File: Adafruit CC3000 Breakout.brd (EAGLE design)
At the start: 39 x 53 mm, 34 parts, among them IC1 ATmega1284P, U1 CC3000MOD, X1 2500AT44M0400E

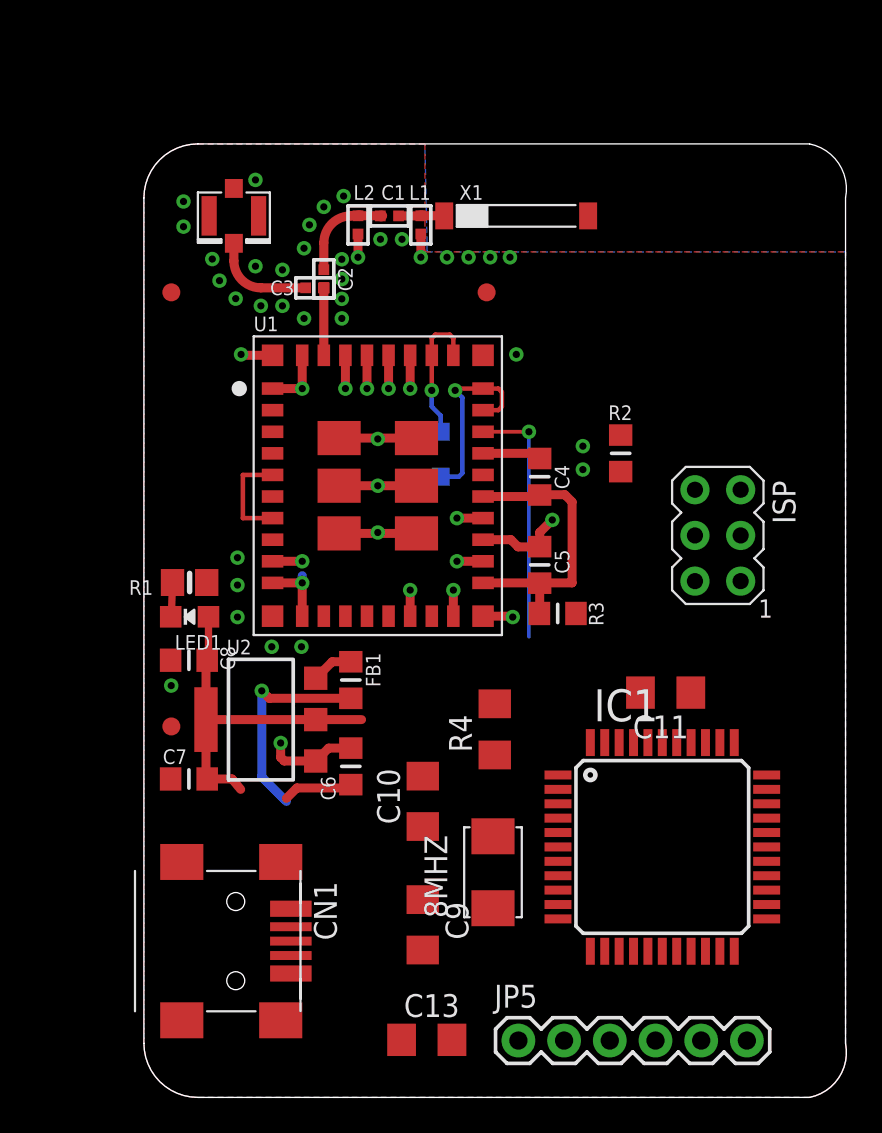
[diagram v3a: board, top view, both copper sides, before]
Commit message: Replace passives (w/ 1206), re-layout components.
Also, change pinouts on the ATmega1284P to match the Wicked Devices
Wildfire prototyping board. Remove rounded corners.
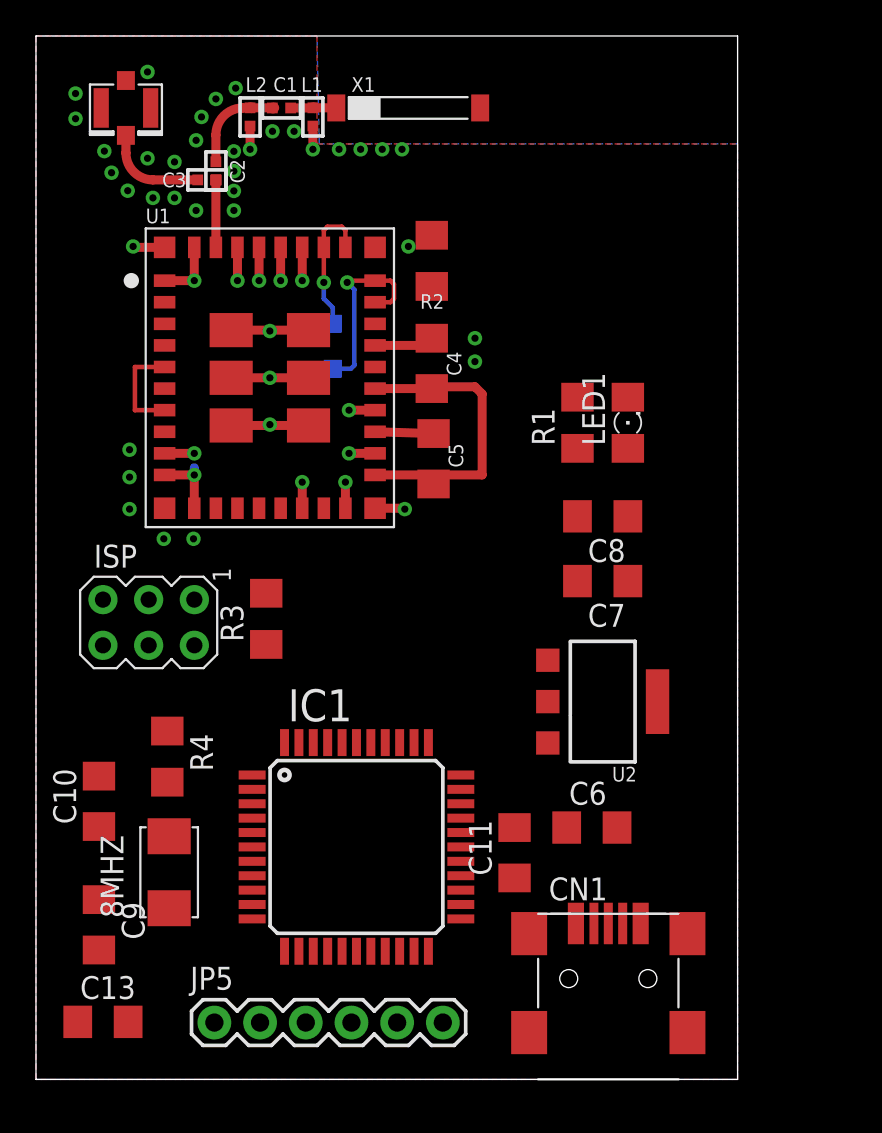
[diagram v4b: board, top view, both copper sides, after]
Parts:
- removed FB1: (no value), microbuilder:_0805MP
- removed FID1, FID2, FID3: FIDUCIAL"", microbuilder:FIDUCIAL_1MM
- C4, C5, C6, C7, C8: device microbuilder:_0805MP -> rcl:C1206
- LED1: device microbuilder:CHIPLED_0805_NOOUTLINE -> led:1206
- R1: device microbuilder:0805-NO -> rcl:R1206
- R2, R3: device microbuilder:_0805MP -> rcl:R1206
- moved ISP 32.0 mm to (6.26, 25.9), turned to 270 degrees
- moved LED1 26.6 mm to (32.9, 37.0)
- moved C7 25.5 mm to (31.5, 28.2)
- moved C8 24.4 mm to (31.5, 31.8)
- moved CN1 23.4 mm to (31.8, 3.83), turned to 0 degrees
- moved R1 23.3 mm to (30.1, 37.0), turned to 90 degrees
- moved U2 19.0 mm to (31.5, 21.5), turned to 270 degrees
- moved R4 18.3 mm to (7.30, 18.4), turned to 270 degrees
- moved C13 18.0 mm to (3.72, 3.70)
- moved 8MHZ 18.0 mm to (7.40, 12.0)
- moved C10 18.0 mm to (3.50, 16.0)
- moved C9 18.0 mm to (3.50, 9.09)
- moved IC1 17.0 mm to (17.8, 13.4)
- moved JP5 16.9 mm to (9.92, 3.66)
- moved R3 16.2 mm to (12.8, 26.1), turned to 90 degrees
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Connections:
- removed net N$9: FB1.2, U2.3
- net SPI_CS_3V: now also IC1.40; no longer IC1.22
- net VBAT_EN_3V: now also IC1.41; no longer IC1.23
- net VIN: now also U2.3; no longer FB1.1
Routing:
- net VBAT: track 36.5 -> 17.2 mm
- net VIN: track 15.7 -> 0.00 mm, vias 1 -> 0
- net VBAT_EN_3V: track 13.9 -> 0.00 mm, vias 1 -> 0
- net GND: track 54.7 -> 47.9 mm, vias 54 -> 51
- net N$9: track 2.33 -> 0.00 mm
- net N$7: track 2.07 -> 0.00 mm
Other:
- board size 39 x 53 mm -> 39 x 58 mm

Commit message: Route board.
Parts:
- moved JP5 2.00 mm to (7.92, 3.66)
- moved C11 0.40 mm to (26.2, 13.1)
- moved R2 0.40 mm to (22.4, 46.0)
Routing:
- net VBAT: track 17.2 -> 106.3 mm, vias 0 -> 2
- net VBAT_EN_3V: track 0.00 -> 44.2 mm, vias 0 -> 2
- net RESET: track 0.00 -> 35.4 mm
- net SPI_CLK_3V: track 0.00 -> 30.1 mm, vias 0 -> 2
- net VIN: track 0.00 -> 30.0 mm
- net SPI_MOSI_3V: track 0.00 -> 21.2 mm, vias 0 -> 2
- net SPI_MISO_3V: track 0.00 -> 20.4 mm, vias 0 -> 2
- net SPI_CS_3V: track 0.00 -> 17.9 mm
- net SPI_IRQ_3V: track 0.00 -> 14.3 mm, vias 0 -> 2
- net N$8: track 0.00 -> 10.6 mm
- net N$10: track 0.00 -> 10.3 mm
- net RX: track 0.00 -> 8.22 mm
- net TX: track 0.00 -> 7.62 mm
- net GND: track 47.9 -> 53.7 mm, vias 51 -> 55
- net DTR: track 0.00 -> 2.86 mm
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
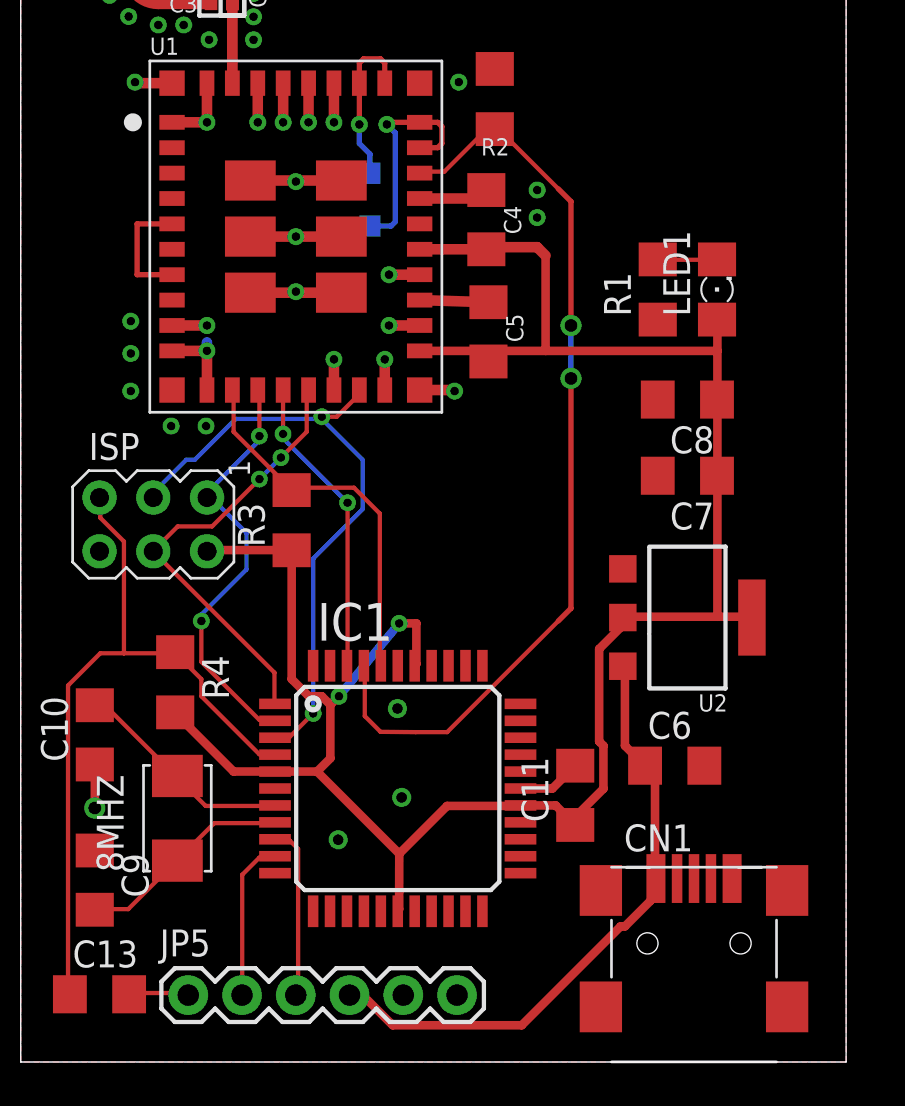
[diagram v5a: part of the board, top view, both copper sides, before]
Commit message: Breakout some microcontroller pins.
Partly un-route the board.
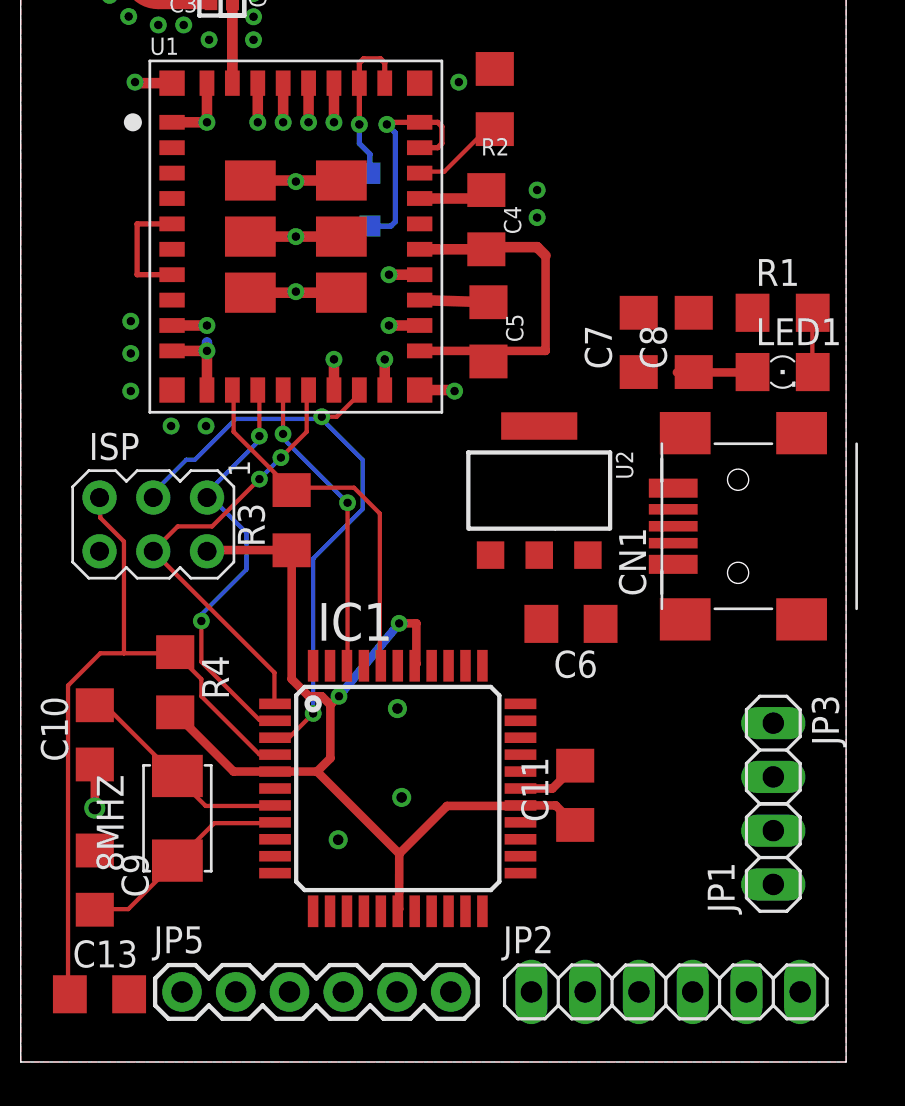
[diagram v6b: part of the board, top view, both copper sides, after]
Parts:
- added JP1, JP3: (no value), pinhead:1X02
- added JP2: (no value), pinhead:1X06
- moved CN1 22.4 mm to (36.2, 25.8), turned to 90 degrees
- moved U2 9.22 mm to (24.5, 27.5), turned to 0 degrees
- moved C6 8.30 mm to (26.0, 21.2), turned to 180 degrees
- moved C7 6.71 mm to (29.2, 34.5), turned to 90 degrees
- moved R1 6.00 mm to (36.0, 35.9), turned to 0 degrees
- moved LED1 4.98 mm to (36.0, 33.1), turned to 0 degrees
- moved C8 2.72 mm to (31.8, 34.5), turned to 90 degrees
- moved JP5 0.33 mm to (7.62, 3.81)
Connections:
- removed net 10: IC1.11
- removed net 11: IC1.12
- removed net 12: IC1.13
- removed net 13: IC1.14
- removed net 16: IC1.19
- removed net 17: IC1.20
- removed net A0: IC1.37
- removed net A1: IC1.36
- new net N$11: IC1.11, JP2.1
- new net N$12: IC1.12, JP2.2
- new net N$13: IC1.13, JP2.3
- new net N$14: IC1.14, JP2.4
- new net N$15: IC1.15, JP2.5
- new net N$16: IC1.16, JP2.6
- new net N$17: IC1.31, JP3.1
- new net N$18: IC1.30, JP3.2
- new net N$5: IC1.19, JP1.1
- new net N$9: IC1.20, JP1.2
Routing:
- net VBAT_EN_3V: track 44.2 -> 4.39 mm, vias 2 -> 0
- net VBAT: track 106.3 -> 70.7 mm
- net VIN: track 30.0 -> 0.00 mm
- net RX: track 8.22 -> 0.00 mm
- net TX: track 7.62 -> 0.00 mm
- net DTR: track 2.86 -> 0.00 mm

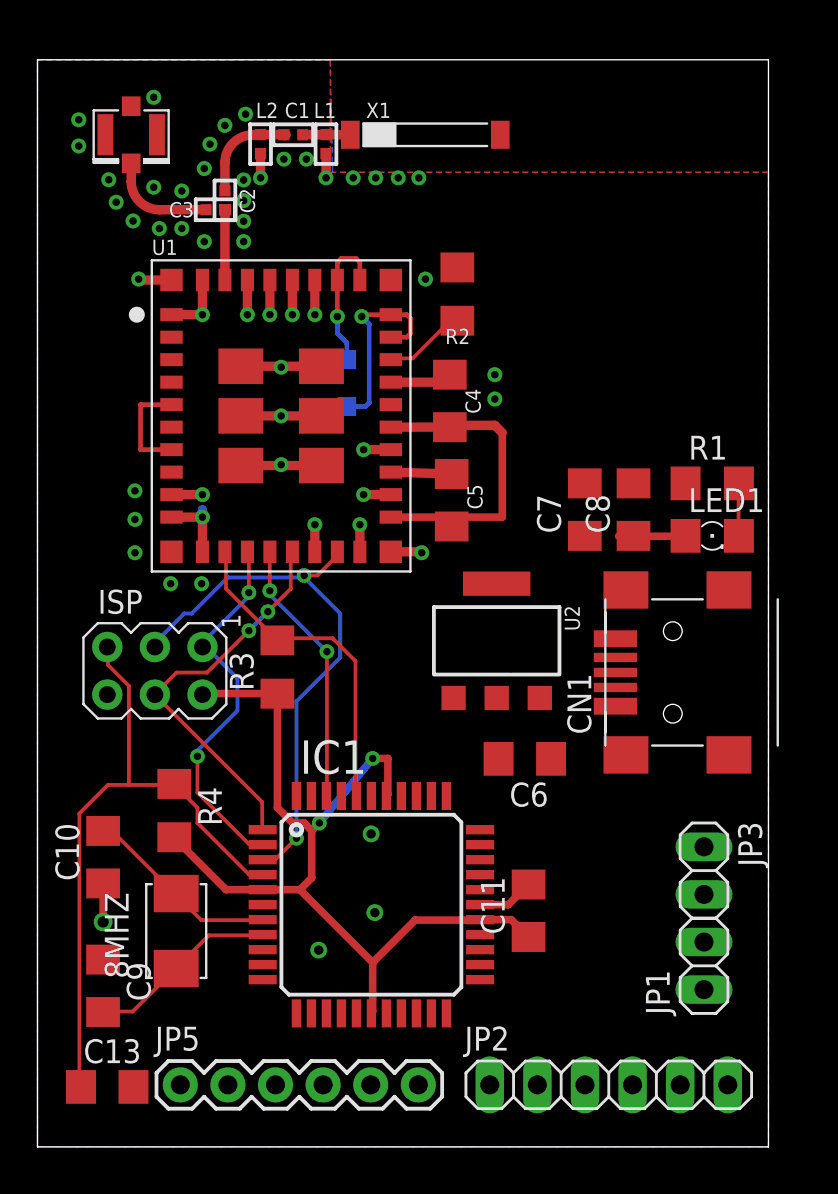
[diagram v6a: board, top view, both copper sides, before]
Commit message: Breakout power and ground. Align to inch grid.
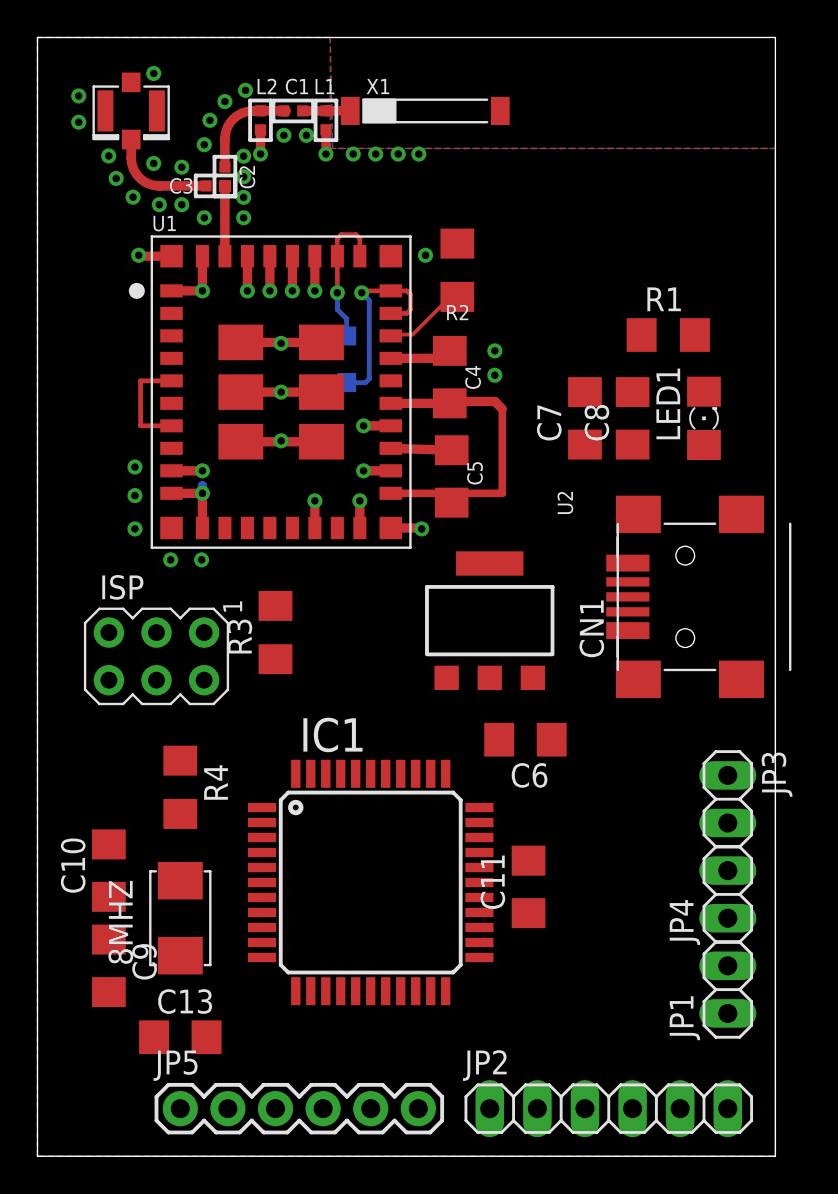
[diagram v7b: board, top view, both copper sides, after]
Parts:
- added JP4: (no value), pinhead:1X02
- moved R1 8.26 mm to (33.7, 43.8)
- moved LED1 6.29 mm to (35.6, 39.4), turned to 90 degrees
- moved C8 4.87 mm to (31.8, 39.4)
- moved C7 4.87 mm to (29.2, 39.4)
- moved C13 4.71 mm to (7.62, 6.35)
- moved CN1 4.09 mm to (36.8, 29.8)
- moved JP3 4.02 mm to (36.8, 19.1)
- moved R3 1.84 mm to (12.7, 27.9)
- moved JP1 1.80 mm to (36.8, 8.89)
- moved R4 1.28 mm to (7.62, 19.7)
- moved C1 1.27 mm to (13.6, 55.8)
- moved C2 1.27 mm to (10.0, 52.3)
- moved C3 1.27 mm to (9.50, 51.8)
- moved C4 1.27 mm to (22.0, 41.6)
- moved C5 1.27 mm to (22.1, 36.3)
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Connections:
- net GND: now also JP4.2
- net VBAT: now also JP4.1
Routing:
- net VBAT: track 70.7 -> 17.6 mm, vias 2 -> 0
- net RESET: track 35.4 -> 0.00 mm
- net SPI_CLK_3V: track 30.1 -> 0.00 mm, vias 2 -> 0
- net SPI_MOSI_3V: track 21.2 -> 0.00 mm, vias 2 -> 0
- net SPI_MISO_3V: track 20.4 -> 0.00 mm, vias 2 -> 0
- net SPI_CS_3V: track 17.9 -> 0.00 mm
- net SPI_IRQ_3V: track 14.3 -> 0.00 mm, vias 2 -> 0
- net N$8: track 10.6 -> 0.06 mm
- net N$10: track 10.3 -> 0.05 mm
- net GND: track 53.7 -> 47.9 mm, vias 55 -> 51
- net N$7: track 2.80 -> 0.00 mm
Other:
- board size 39 x 58 mm -> 39.4 x 59.7 mm
